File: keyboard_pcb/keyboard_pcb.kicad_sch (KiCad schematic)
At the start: 0 parts

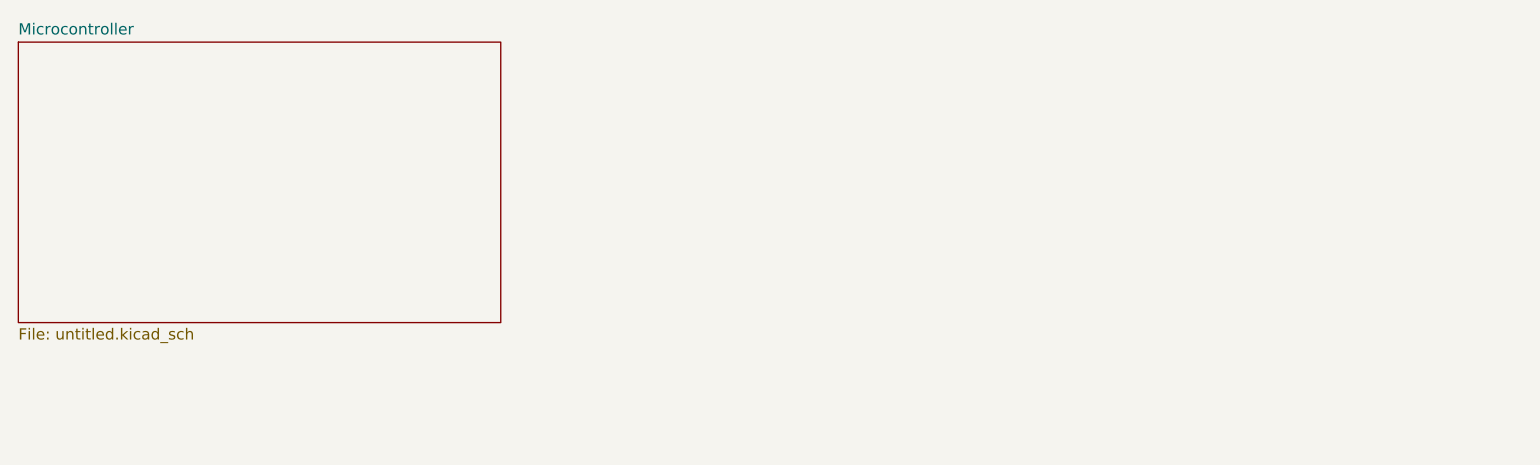
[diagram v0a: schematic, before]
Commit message: implemented matrix
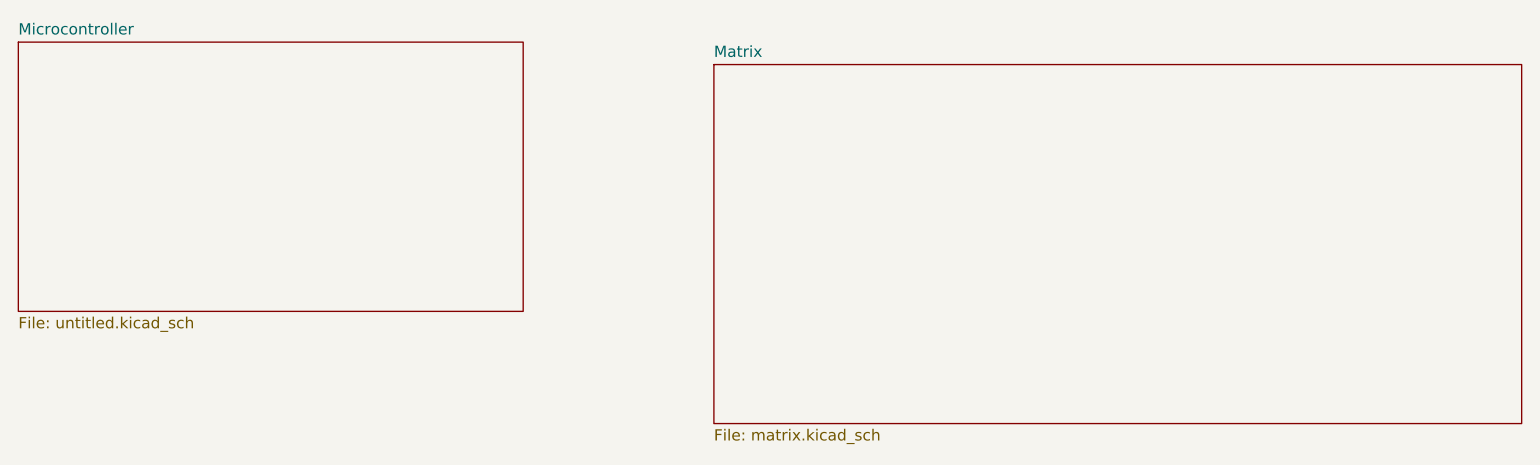
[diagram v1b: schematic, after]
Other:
- added sheet Matrix (matrix.kicad_sch)
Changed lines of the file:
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@@
 	(sheet
 		(at 21.59 21.59)
-		(size 54.61 31.75)
+		(size 57.15 30.48)
 		(fields_autoplaced yes)
 		(stroke
@@
 		)
 		(property "Sheetfile" "untitled.kicad_sch"
-			(at 21.59 53.9246 0)
+			(at 21.59 52.6546 0)
 			(effects
 				(font
@@
 				)
 			)
+		)
+	)
+	(sheet
+		(at 100.33 24.13)
+		(size 91.44 40.64)
+		(fields_autoplaced yes)
+		(stroke
+			(width 0.1524)
+			(type solid)
+		)
+		(fill
+			(color 0 0 0 0.0000)
+		)
+		(property "Sheetname" "Matrix"
+			(at 100.33 23.4184 0)
+			(effects
+				(font
+					(size 1.27 1.27)
+				)
+				(justify left bottom)
+			)
+		)
+		(property "Sheetfile" "matrix.kicad_sch"
+			(at 100.33 65.3546 0)
+			(effects
+				(font
+					(size 1.27 1.27)
+				)
+				(justify left top)
+			)
+		)
+		(instances
+			(project "keyboard_pcb"
+				(path "/5a0b976f-d314-4fca-8ab0-732ea8a514fc"
+					(page "3")
+				)
+			)

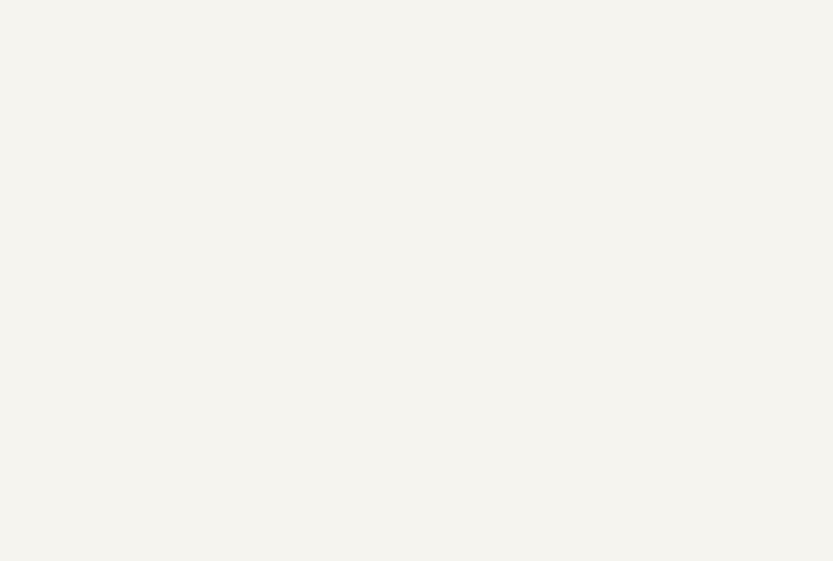
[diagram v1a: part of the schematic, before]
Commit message: implemented LEDs and switch and diode layout
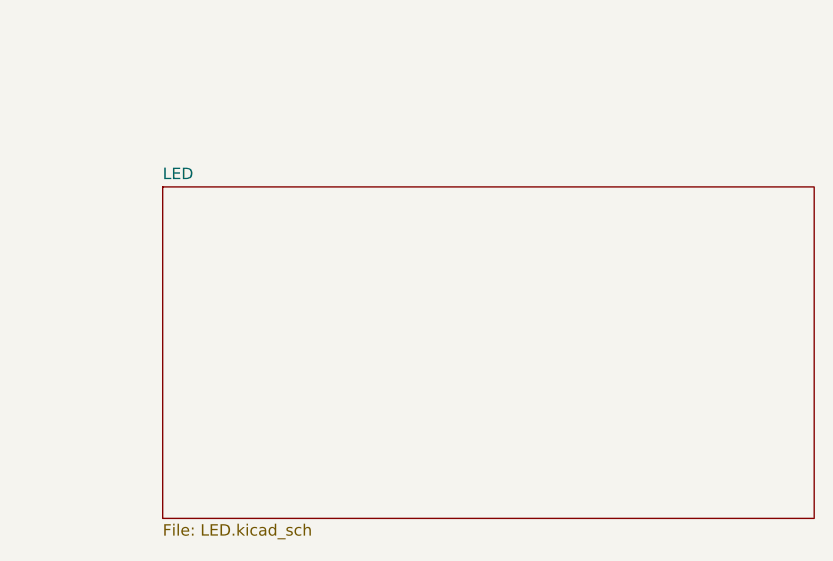
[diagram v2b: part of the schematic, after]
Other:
- added sheet LED (LED.kicad_sch)
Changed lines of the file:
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@@
+	)
+	(sheet
+		(at 121.92 90.17)
+		(size 72.39 36.83)
+		(fields_autoplaced yes)
+		(stroke
+			(width 0.1524)
+			(type solid)
+		)
+		(fill
+			(color 0 0 0 0.0000)
+		)
+		(property "Sheetname" "LED"
+			(at 121.92 89.4584 0)
+			(effects
+				(font
+					(size 1.27 1.27)
+				)
+				(justify left bottom)
+			)
+		)
+		(property "Sheetfile" "LED.kicad_sch"
+			(at 121.92 127.5846 0)
+			(effects
+				(font
+					(size 1.27 1.27)
+				)
+				(justify left top)
+			)
+		)
+		(instances
+			(project "keyboard_pcb"
+				(path "/5a0b976f-d314-4fca-8ab0-732ea8a514fc"
+					(page "4")
+				)
+			)
+		)
 	)
 	(sheet

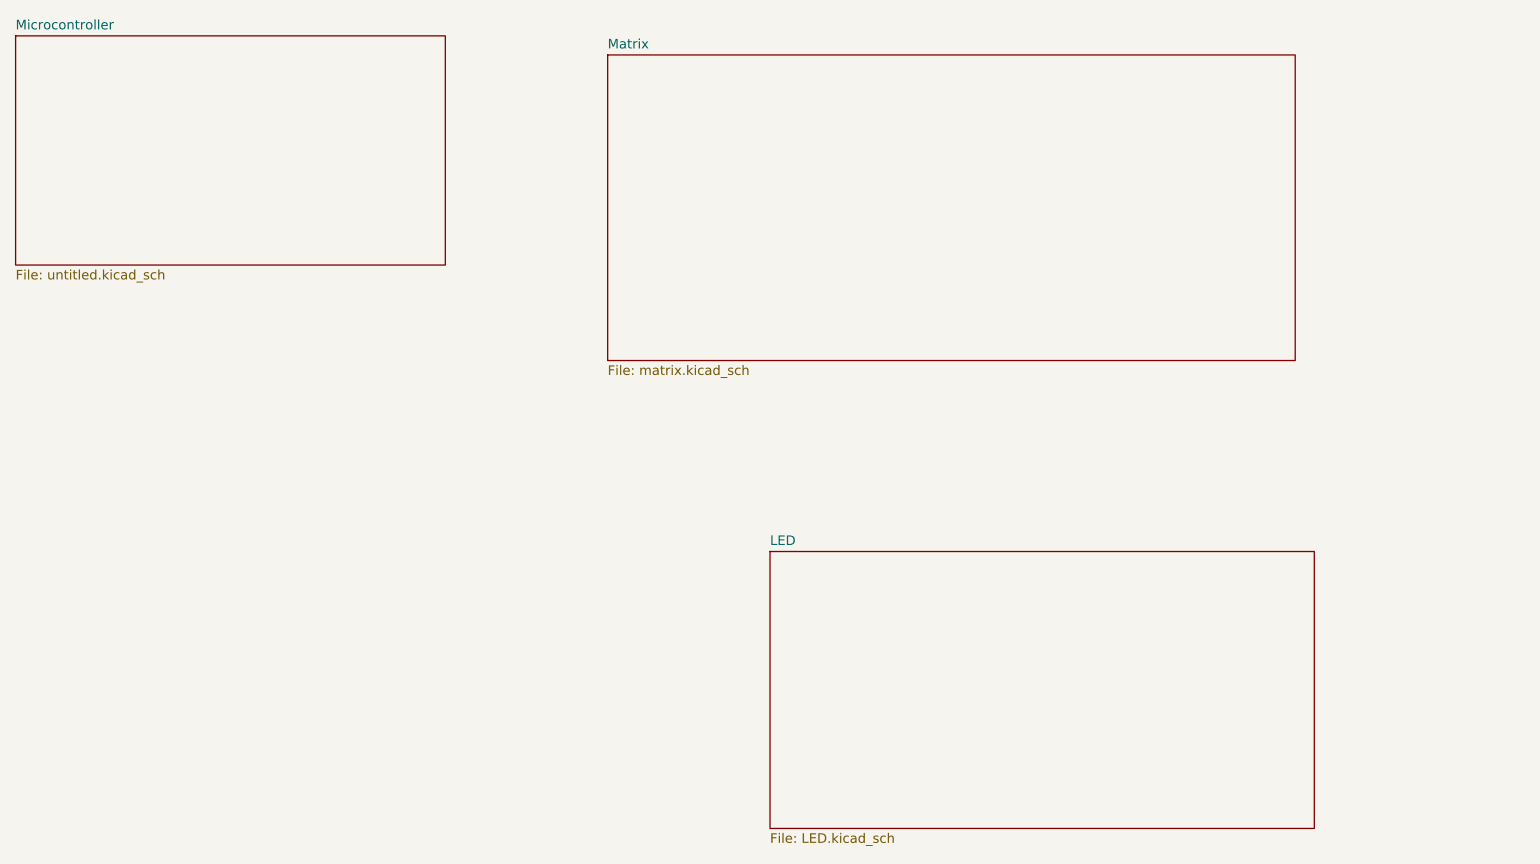
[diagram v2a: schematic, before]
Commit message: added led capacitors and route all leds
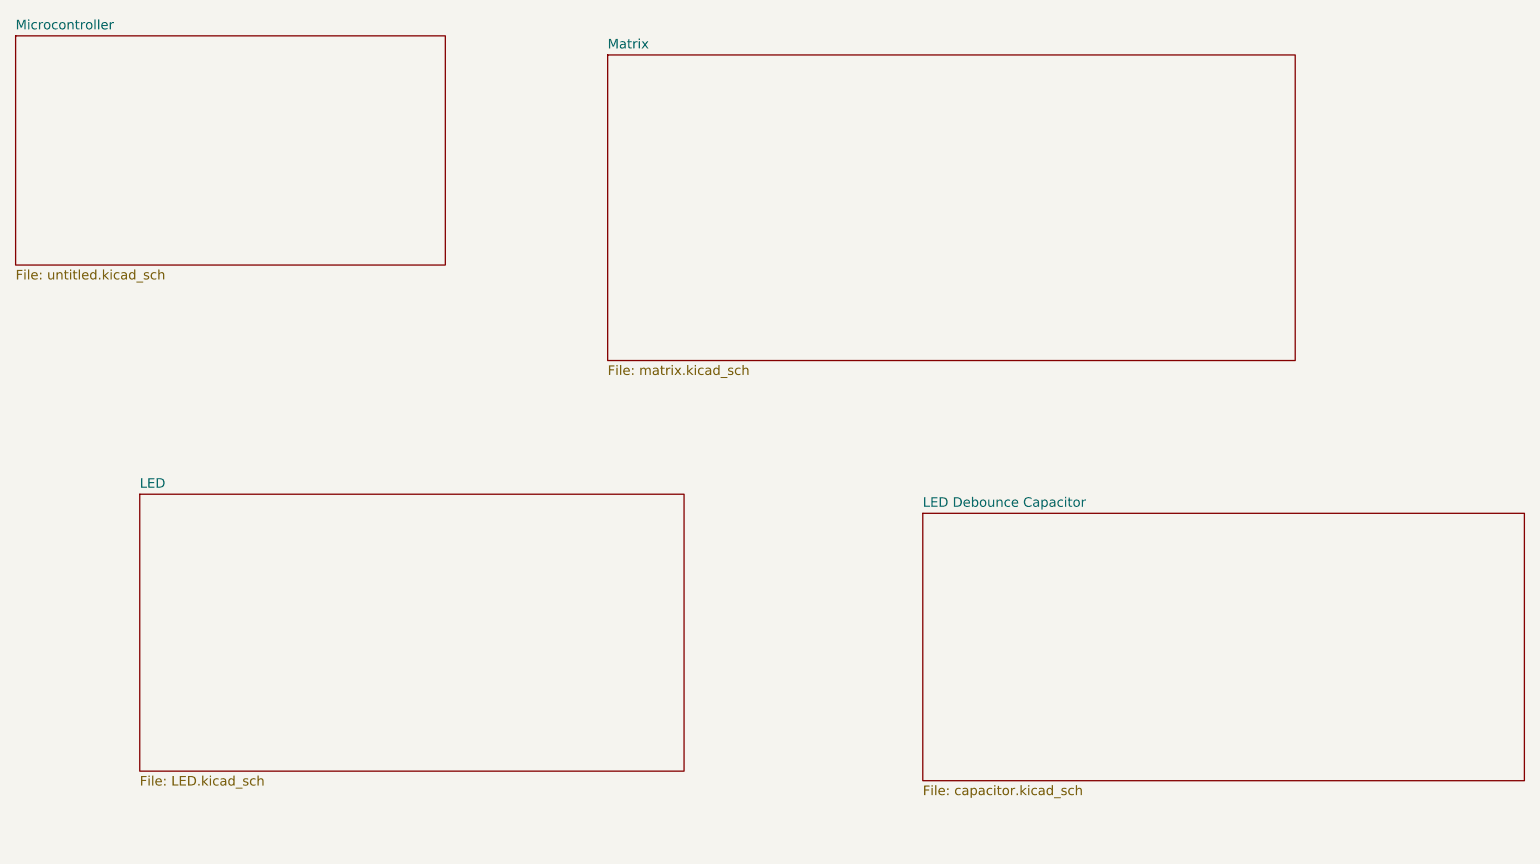
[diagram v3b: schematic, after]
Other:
- added sheet LED Debounce Capacitor (capacitor.kicad_sch)
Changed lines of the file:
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@@
 	(paper "A4")
+	(sheet
+		(at 142.24 85.09)
+		(size 80.01 35.56)
+		(fields_autoplaced yes)
+		(stroke
+			(width 0.1524)
+			(type solid)
+		)
+		(fill
+			(color 0 0 0 0.0000)
+		)
+		(property "Sheetname" "LED Debounce Capacitor"
+			(at 142.24 84.3784 0)
+			(effects
+				(font
+					(size 1.27 1.27)
+				)
+				(justify left bottom)
+			)
+		)
+		(property "Sheetfile" "capacitor.kicad_sch"
+			(at 142.24 121.2346 0)
+			(effects
+				(font
+					(size 1.27 1.27)
+				)
+				(justify left top)
+			)
+		)
+		(instances
+			(project "keyboard_pcb"
+				(path "/5a0b976f-d314-4fca-8ab0-732ea8a514fc"
+					(page "5")
+				)
+			)
+		)
+	)
 	(sheet
 		(at 21.59 21.59)
@@
 	)
 	(sheet
-		(at 121.92 90.17)
+		(at 38.1 82.55)
 		(size 72.39 36.83)
 		(fields_autoplaced yes)
@@
 		)
 		(property "Sheetname" "LED"
-			(at 121.92 89.4584 0)
+			(at 38.1 81.8384 0)
 			(effects
 				(font
@@
 		)
 		(property "Sheetfile" "LED.kicad_sch"
-			(at 121.92 127.5846 0)
+			(at 38.1 119.9646 0)
 			(effects
 				(font
